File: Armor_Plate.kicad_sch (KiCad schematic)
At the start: 46 parts, among them SW3 SW_SP3T

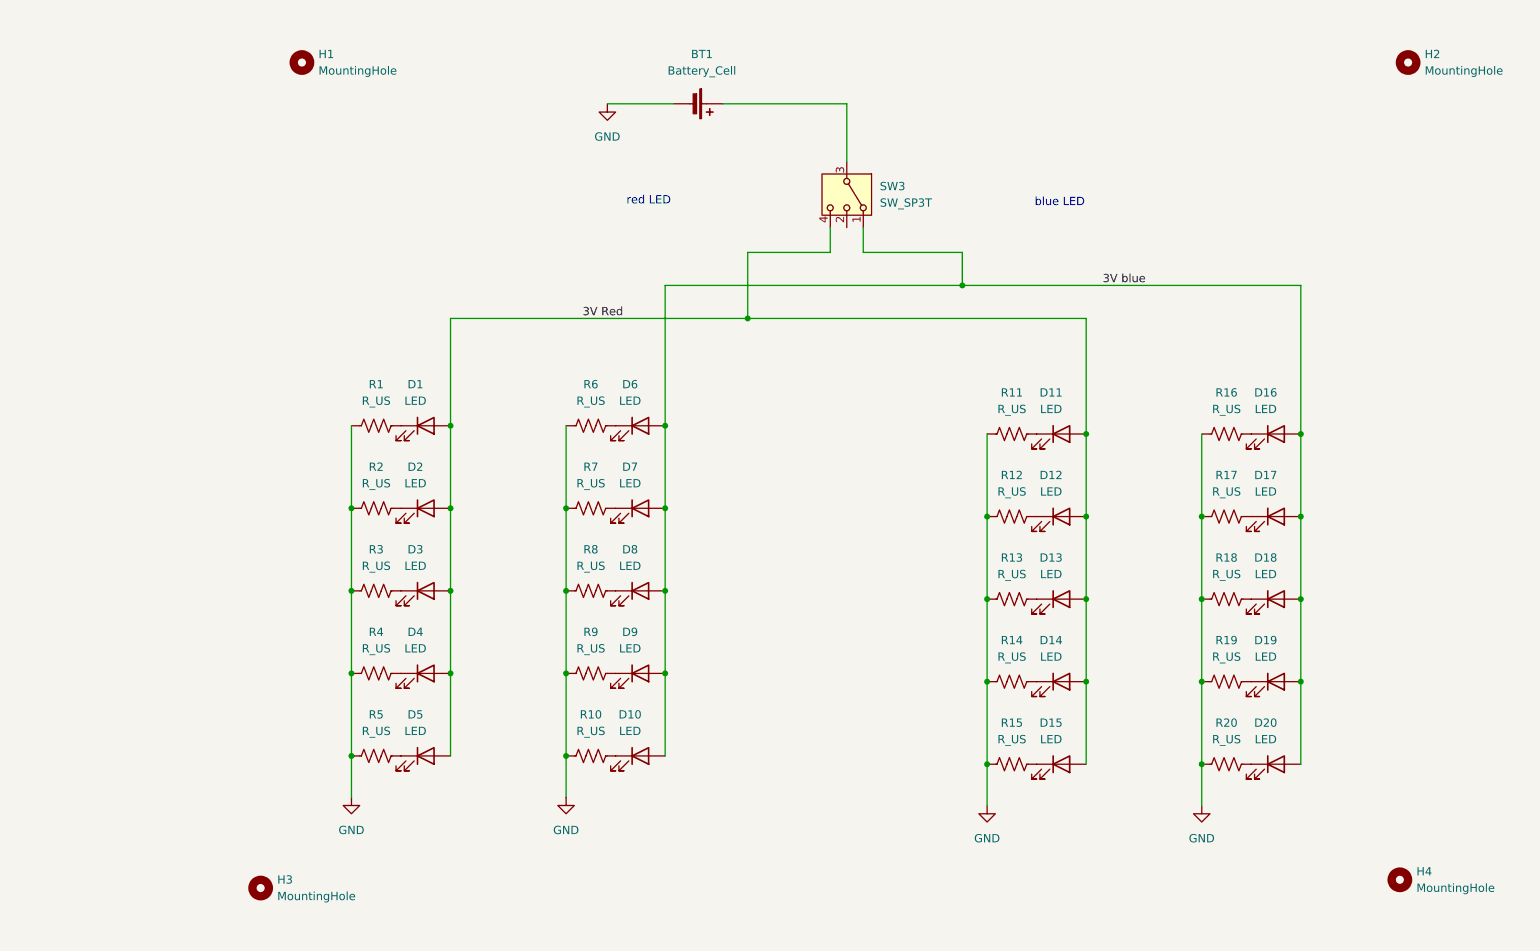
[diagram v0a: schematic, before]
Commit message: Staged work for Armor Plate team
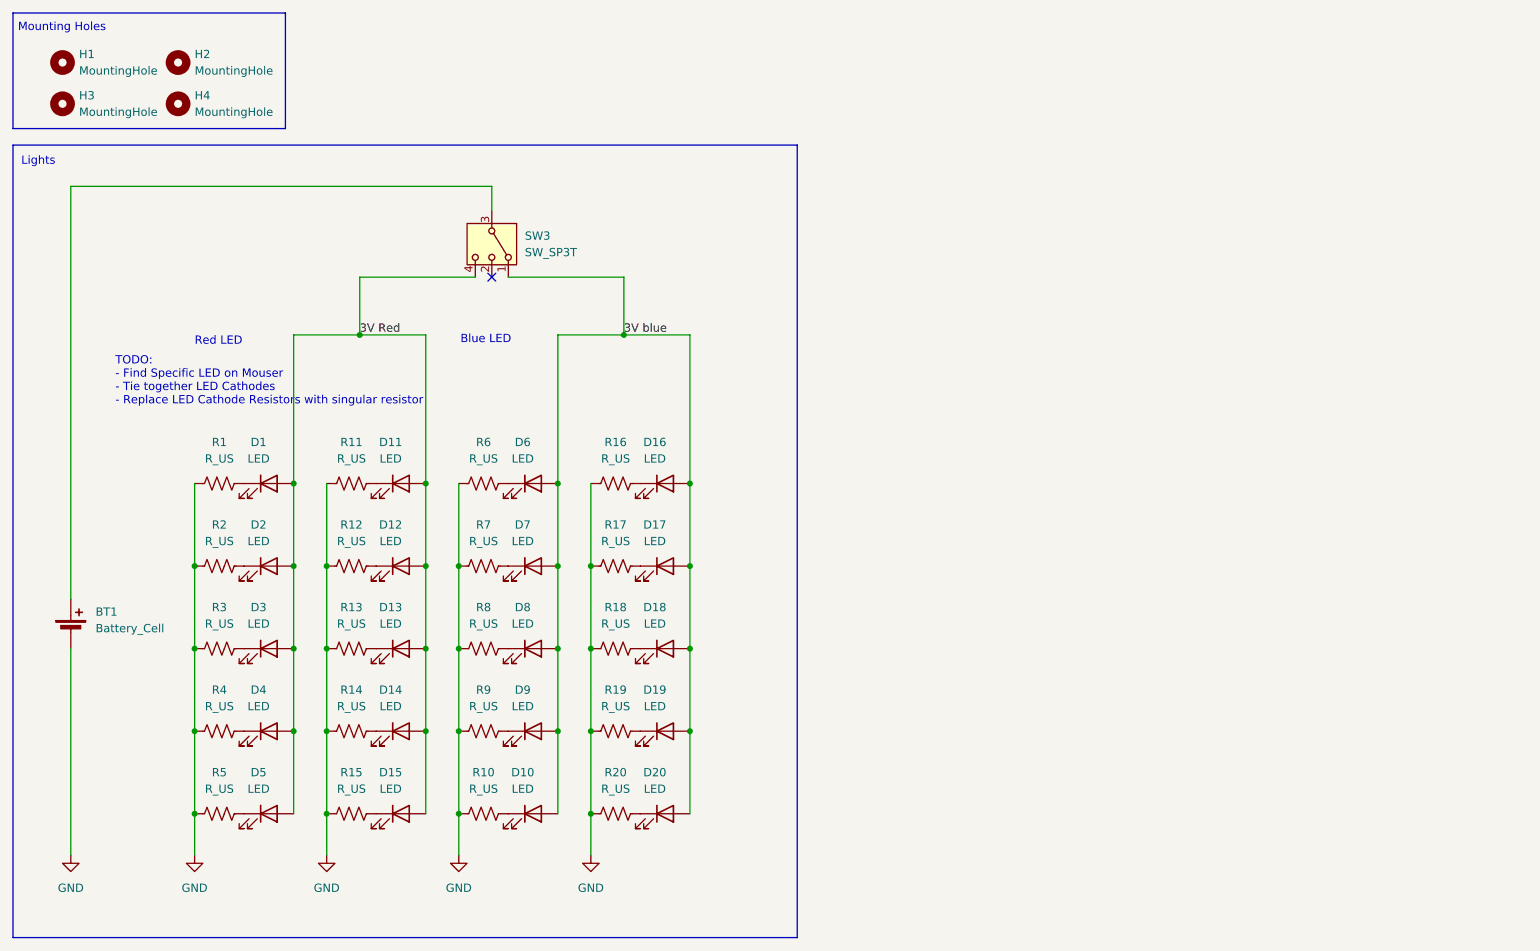
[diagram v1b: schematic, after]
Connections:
- no-connect marks 0 -> 1
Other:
- note added: "Blue LED"
- note added: "Lights"
- note added: "Mounting Holes"
- note added: "Red LED"
- note added: "TODO: - Find Specific LED on Mouser - Tie together LED Cathodes - Replace LED Cathode Resistors with singular resistor"
- note removed: "blue LED"
- note removed: "red LED"
- company: (none) -> UT IEEE RAS - Stampede
- title: (none) -> Armor Plate Mockup
- moved on the sheet: BT1, D1, D10, D11, D12, D13, D14, D15, D16, D17, D18, D19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
